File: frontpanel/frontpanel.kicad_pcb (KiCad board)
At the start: 2 copper layers, 80.9 x 128.5 mm, 3 parts

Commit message: holes completed on frontpanel
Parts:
- moved REF** 2.39 mm to (109.8, 113.2)
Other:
- outline, holes or cut-outs redrawn
- board text added: "Ilse"
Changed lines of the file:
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@@
       (layer "B.Paste" (type "Bottom Solder Paste"))
       (layer "B.SilkS" (type "Bottom Silk Screen"))
-      (copper_finish "None")
+      (copper_finish "HAL lead-free")
       (dielectric_constraints no)
     )
@@
   )
   (net 0 "")
-  (footprint "CHAIR:MountingHole_Eurorack_3U_slotted" (layer "F.Cu")
+  (footprint "CHAIR:MountingHole_Eurorack_3U_slotted" locked (layer "F.Cu")
     (at 135.342 36.83)
     (descr "Pair of Eurorack Mounting slotted holes in 3U height")
@@
       (effects (font (size 1 1) (thickness 0.15)))
     )
-    (fp_text user "7.5mm" (at -4 69 unlocked) (layer "Cmts.User")
+    (fp_text user "7.5mm" (at 4 130 unlocked) (layer "Cmts.User")
       (effects (font (size 1 1) (thickness 0.15)))
     )
@@
       (effects (font (size 1 1) (thickness 0.15)))
     )
-    (fp_text user "128.5mm" (at -9 55.5 90 unlocked) (layer "Cmts.User")
+    (fp_text user "128.5mm" (at -1.75 115.25 90 unlocked) (layer "Cmts.User")
       (effects (font (size 1 1) (thickness 0.15)))
     )
@@
     )
   )
-  (footprint "CHAIR:MountingHole_Eurorack_3U_slotted" (layer "F.Cu")
+  (footprint "CHAIR:MountingHole_Eurorack_3U_slotted" locked (layer "F.Cu")
     (at 69.342 36.83)
     (descr "Pair of Eurorack Mounting slotted holes in 3U height")
@@
       (effects (font (size 1 1) (thickness 0.15)))
     )
-    (fp_text user "128.5mm" (at -9 55.5 90 unlocked) (layer "Cmts.User")
+    (fp_text user "128.5mm" (at -1.75 115.5 90 unlocked) (layer "Cmts.User")
       (effects (font (size 1 1) (thickness 0.15)))
     )
@@
       (effects (font (size 1 1) (thickness 0.15)))
     )
-    (fp_text user "3mm" (at 6 66 unlocked) (layer "Cmts.User")
+    (fp_text user "3mm" (at 13.25 1.5 unlocked) (layer "Cmts.User")
       (effects (font (size 1 1) (thickness 0.15)))
     )
@@
     )
   )
-  (footprint "mainboard:ilse-main-board" (layer "F.Cu")
-    (at 109.342 110.83)
+  (footprint "mainboard:ilse-main-board" locked (layer "F.Cu")
+    (at 109.792 113.18)
     (attr smd)
-    (fp_text reference "REF**" (at 0 -4 unlocked) (layer "F.SilkS")
-      (effects (font (size 1 1) (thickness 0.15)))
-    )
-    (fp_text value "ilse-main-board" (at 0 -2.5 unlocked) (layer "F.Fab")
-      (effects (font (size 1 1) (thickness 0.15)))
-    )
-    (fp_text user "${REFERENCE}" (at 0 -1 unlocked) (layer "F.Fab")
+    (fp_text reference "REF**" (at 1 -5.5 unlocked) (layer "F.SilkS") hide
+      (effects (font (size 1 1) (thickness 0.15)))
+    )
+    (fp_text value "ilse-main-board" (at 1 -4 unlocked) (layer "F.Fab")
+      (effects (font (size 1 1) (thickness 0.15)))
+    )
+    (fp_text user locked "${REFERENCE}" (at 1 -2.5 unlocked) (layer "F.Fab")
       (effects (font (size 1 1) (thickness 0.15)))
     )
@@
   )
   (gr_rect (start 69.342 36.83) (end 150.242 165.354) (layer "Edge.Cuts") (width 0.1) (fill none))
+  (gr_circle (center 80.16 96.256) (end 83.26 96.256) (layer "Edge.Cuts") (width 0.1) (fill none))
+  (gr_circle (center 100.27 120.966) (end 103.37 120.966) (layer "Edge.Cuts") (width 0.1) (fill none))
+  (gr_circle (center 80.32 71.366) (end 83.42 71.366) (layer "Edge.Cuts") (width 0.1) (fill none))
+  (gr_circle (center 110.28 96.166) (end 113.38 96.166) (layer "Edge.Cuts") (width 0.1) (fill none))
+  (gr_circle (center 140.3 71.386) (end 143.4 71.386) (layer "Edge.Cuts") (width 0.1) (fill none))
+  (gr_circle (center 140.266 120.966) (end 143.366 120.966) (layer "Edge.Cuts") (width 0.1) (fill none))
+  (gr_circle (center 130.27 120.966) (end 133.37 120.966) (layer "Edge.Cuts") (width 0.1) (fill none))
+  (gr_circle (center 110.31 71.386) (end 113.41 71.386) (layer "Edge.Cuts") (width 0.1) (fill none))
+  (gr_circle (center 110.27 120.966) (end 113.37 120.966) (layer "Edge.Cuts") (width 0.1) (fill none))
+  (gr_circle (center 124.66 53.071) (end 127.76 53.071) (layer "Edge.Cuts") (width 0.1) (fill none))
+  (gr_circle (center 94.91 53.061) (end 98.01 53.061) (layer "Edge.Cuts") (width 0.1) (fill none))
+  (gr_circle (center 120.27 120.966) (end 123.37 120.966) (layer "Edge.Cuts") (width 0.1) (fill none))
+  (gr_circle (center 140.356 86.346) (end 142.906 86.346) (layer "Edge.Cuts") (width 0.1) (fill none))
+  (gr_circle (center 140.27 96.166) (end 143.37 96.166) (layer "Edge.Cuts") (width 0.1) (fill none))
+  (gr_circle (center 80.32 121.266) (end 83.42 121.266) (layer "Edge.Cuts") (width 0.1) (fill none))
+  (gr_circle (center 110.246 53.416) (end 112.796 53.416) (layer "Edge.Cuts") (width 0.1) (fill none))
+  (gr_line (start 149.52 165.33) (end 151.02 165.33) (layer "User.1") (width 0.1))
+  (gr_line (start 150.222 166.08) (end 150.222 164.58) (layer "User.1") (width 0.1))
+  (gr_line (start 149.52 165.33) (end 151.02 165.33) (layer "User.1") (width 0.1))
+  (gr_line (start 150.246 166.08) (end 150.246 164.58) (layer "User.1") (width 0.1))
+  (gr_line (start 149.52 165.33) (end 151.02 165.33) (layer "User.1") (width 0.1))
+  (gr_line (start 150.246 166.08) (end 150.246 164.58) (layer "User.1") (width 0.1))
+  (gr_line (start 149.496 165.33) (end 150.996 165.33) (layer "User.1") (width 0.1))
+  (gr_line (start 150.246 166.08) (end 150.246 164.58) (layer "User.1") (width 0.1))
+  (gr_text "Ilse" (at 109.342 161.33) (layer "F.Mask")
+    (effects (font (size 5 5) (thickness 0.3) italic))
+  )
+  (dimension (type orthogonal) (layer "Dwgs.User")
+    (pts (xy 145.342 165.33) (xy 144.842 36.83))
+    (height 13.5)
+    (orientation 1)
+    (gr_text "128,5 mm" (at 157.692 101.08 90) (layer "Dwgs.User")
+      (effects (font (size 1 1) (thickness 0.15)))
+    )
+    (format (units 2) (units_format 1) (precision 2) suppress_zeroes)
+    (style (thickness 0.15) (arrow_length 1.27) (text_position_mode 0) (extension_height 0.58642) (extension_offset 0.5) keep_text_aligned)
+  )
+  (dimension (type orthogonal) (layer "Dwgs.User")
+    (pts (xy 150.242 162.33) (xy 69.342 163.33))
+    (height 10.5)
+    (orientation 0)
+    (gr_text "80,9 mm" (at 109.792 171.68) (layer "Dwgs.User")
+      (effects (font (size 1 1) (thickness 0.15)))
+    )
+    (format (units 2) (units_format 1) (precision 4) suppress_zeroes)
+    (style (thickness 0.15) (arrow_length 1.27) (text_position_mode 0) (extension_height 0.58642) (extension_offset 0.5) keep_text_aligned)
+  )
+  (group "" (id 4550d7ba-dc8a-45d7-aaa6-15a4197e74b3)
+    (members
+      b2d435cb-ca23-4e81-9a5f-00ce2d6e939f
+      e1e0012c-160d-4635-8a2e-343ac09a54ce
+    )
+  )
+  (group "" (id 53f20b6f-ed63-4e61-9c39-1de7fdf3f633)
+    (members
+      769fc36e-3c89-4daf-9fb8-d31f41f09f12
+      9d5866f7-7d4c-4051-aae8-ac6ee581d4aa
+    )
+  )
+  (group "" (id 62ab9210-0277-4024-b203-94644154249a)
+    (members
+      60aee7a8-f06c-4d6f-ba96-c595e4d3ce01
+      bdc38be8-cc61-4140-b369-775a143d4fe8
+    )
+  )
+  (group "" (id 7d65d4cc-69c7-4c5b-9f9c-142ebdf7d3cf)
+    (members
+      6b8d4cce-d73b-4a16-8d6f-51582b9856b5
+      d6c208ab-7223-426a-ae88-94b22786bc94
+    )
+  )
 )

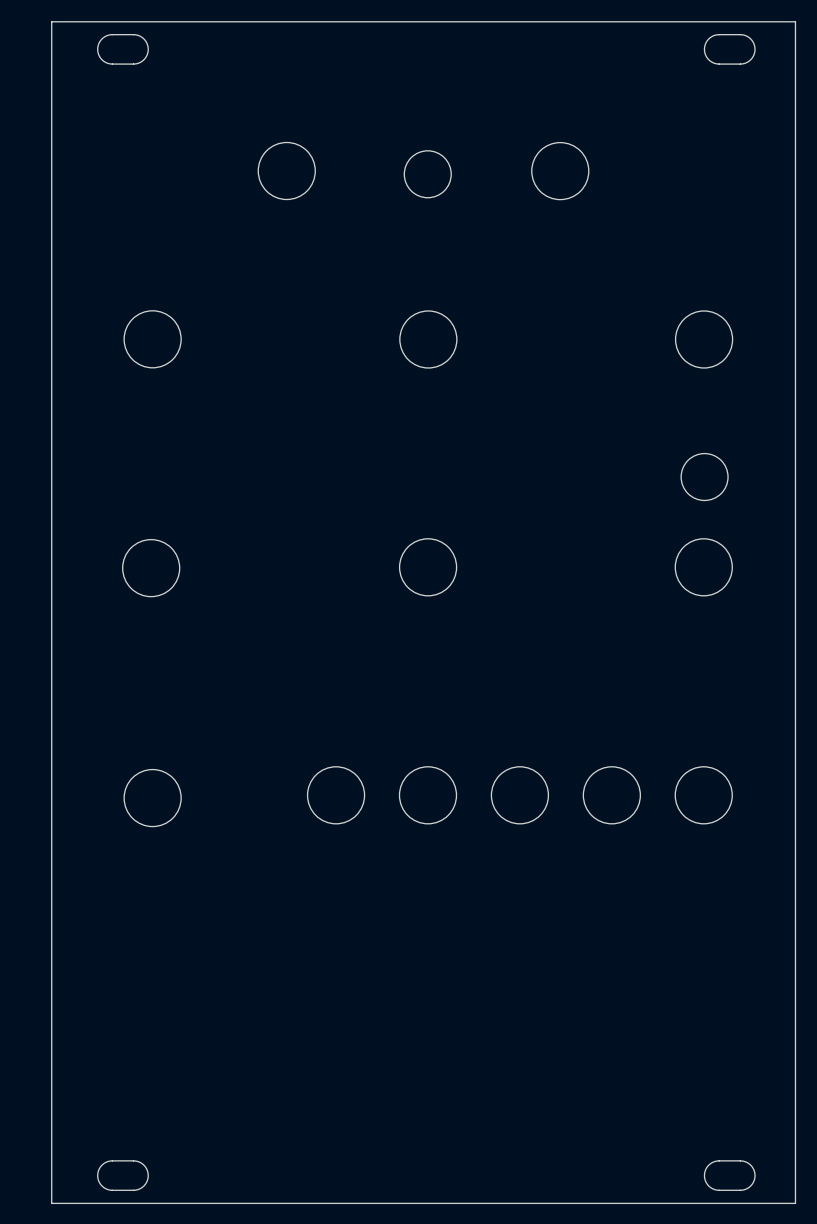
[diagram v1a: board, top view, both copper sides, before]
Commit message: frontpanel functional, CV input GND added
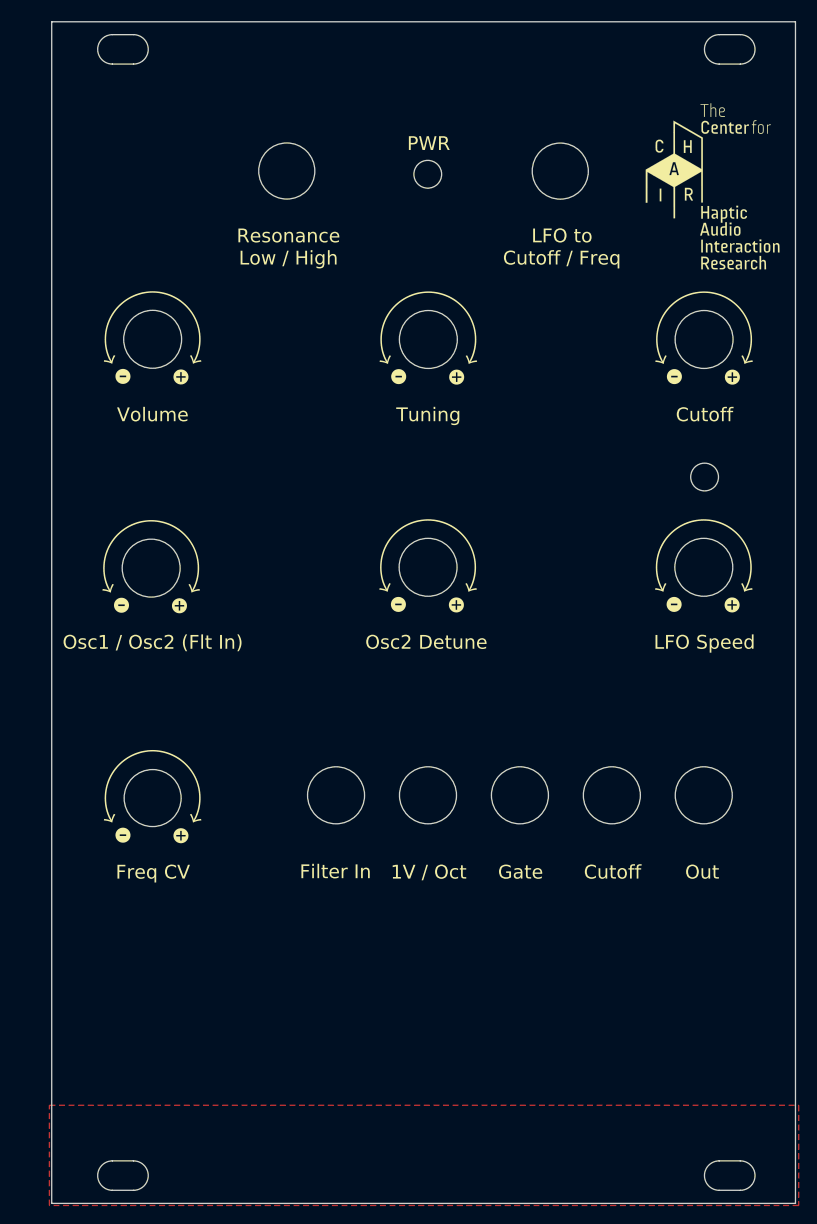
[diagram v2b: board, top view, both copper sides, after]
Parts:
- added LOGO1: CHAIR-LOGO, CHAIR:CHAIR_logo_silkscreen, F.Cu at (141.2, 54.7)
- added REF**: SONGHUEI_R0904N_MountingHole_6.3mm_Silkscreen+-, CHAIR:SONGHUEI_R0904N_NoHole_Silkscreen-+, F.Cu at (140.3, 71.4)
- added REF**: SONGHUEI_R0904N_MountingHole_6.3mm_Silkscreen+-, CHAIR:SONGHUEI_R0904N_NoHole_Silkscreen-+, F.Cu at (80.2, 96.3)
- added REF**: SONGHUEI_R0904N_MountingHole_6.3mm_Silkscreen+-, CHAIR:SONGHUEI_R0904N_NoHole_Silkscreen-+, F.Cu at (80.3, 71.4)
- added REF**: SONGHUEI_R0904N_MountingHole_6.3mm_Silkscreen+-, CHAIR:SONGHUEI_R0904N_NoHole_Silkscreen-+, F.Cu at (140.3, 96.2)
- added REF**: SONGHUEI_R0904N_MountingHole_6.3mm_Silkscreen+-, CHAIR:SONGHUEI_R0904N_NoHole_Silkscreen-+, F.Cu at (110.3, 96.2)
- added REF**: SONGHUEI_R0904N_MountingHole_6.3mm_Silkscreen+-, CHAIR:SONGHUEI_R0904N_NoHole_Silkscreen-+, F.Cu at (80.3, 121.3)
- added REF**: SONGHUEI_R0904N_MountingHole_6.3mm_Silkscreen+-, CHAIR:SONGHUEI_R0904N_NoHole_Silkscreen-+, F.Cu at (110.3, 71.4)
- H1: value MountingHole -> Eurorack Mounting hole pair left
- H2: value MountingHole -> Eurorack Mounting hole pair right
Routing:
- added copper zone on F.Cu, net (none)
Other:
- outline, holes or cut-outs redrawn
- board text added: "1V / Oct"
- board text added: "Cutoff"
- board text added: "Filter In"
- board text added: "Freq CV"
- board text added: "Gate"
- board text added: "LFO Speed"
- board text added: "LFO to Cutoff / Freq"
- board text added: "Osc1 / Osc2 (Flt In)"
- board text added: "Osc2 Detune"
- board text added: "Out"
- board text added: "PWR"
- board text added: "Resonance Low / High"
- board text added: "Tuning"
- board text added: "Volume"

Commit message: ready for review
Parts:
- removed LOGO1: CHAIR-LOGO, CHAIR:CHAIR_logo_silkscreen
- added G***: LOGO, CHAIR:CHAIR_logo_horizontal_silkscreen+Cu, F.Cu at (109.9, 158.5)
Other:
- outline, holes or cut-outs redrawn
- board text added: "Freq"
- board text added: "High"
- board text added: "LFO →"
- board text added: "Low"
- board text added: "Resonance"
- board text added: "↑ 1V / Oct"
- board text added: "↑ Cutoff"
- board text added: "↑ Filter"
- board text added: "↑ Gate"
- board text added: "↓ Out"
- board text removed: "1V / Oct"
- board text removed: "Filter In"
- board text removed: "Gate"
- board text removed: "LFO to Cutoff / Freq"
- board text removed: "Out"
- board text removed: "Resonance Low / High"

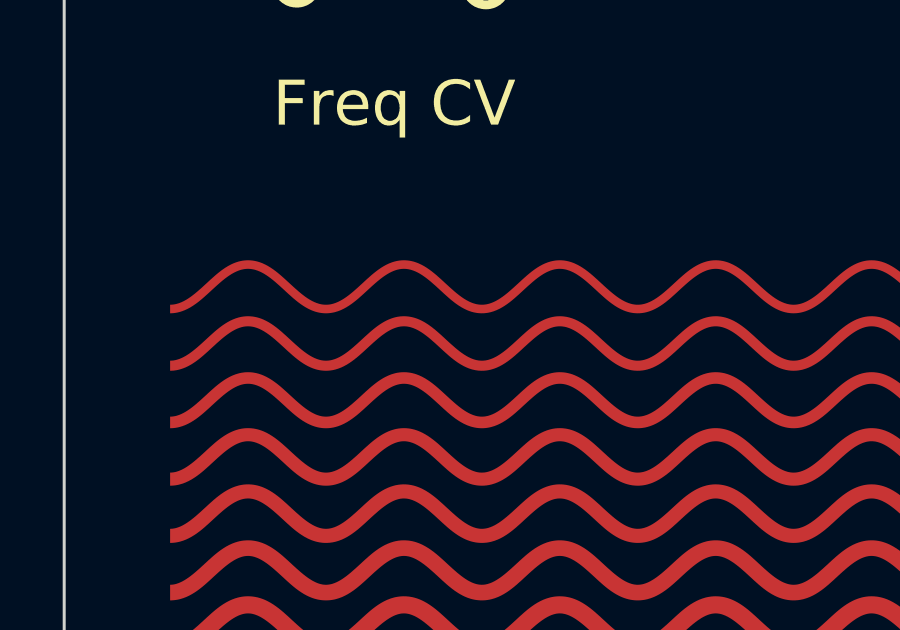
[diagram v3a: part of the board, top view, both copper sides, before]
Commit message: JLCJLCJLCJLC added to PCBs
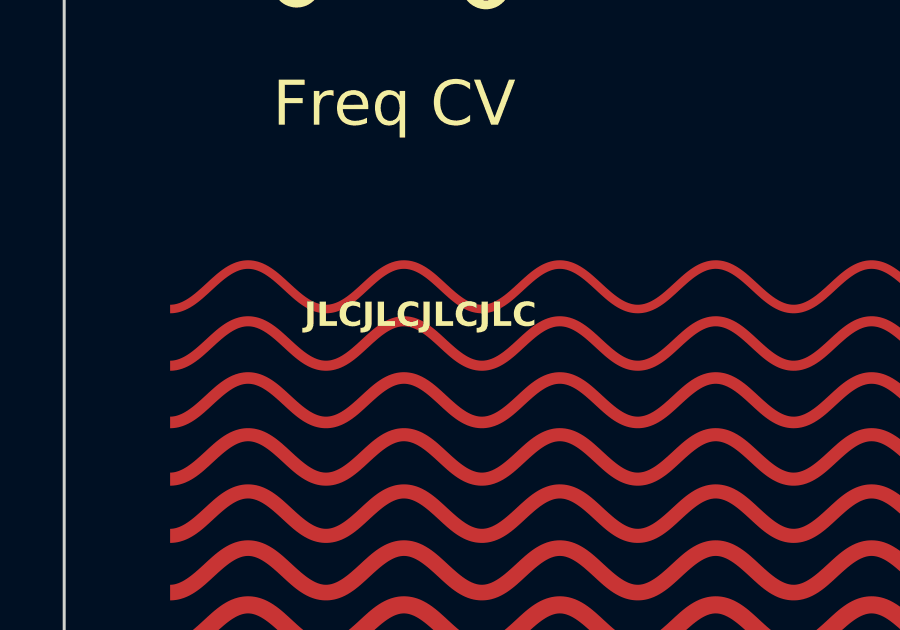
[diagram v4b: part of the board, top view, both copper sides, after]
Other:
- board text added: "JLCJLCJLCJLC"
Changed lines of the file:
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@@
     )
+  )
+  (gr_text "JLCJLCJLCJLC" (at 77.342 136.83) (layer "F.SilkS")
+    (effects (font (size 0.81 0.81) (thickness 0.151) bold) (justify left bottom))
   )
   (gr_text "Cutoff" (at 128.842 57.58) (layer "F.SilkS")
